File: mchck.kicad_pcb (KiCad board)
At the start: 2 copper layers, 36.6 x 18.8 mm, 41 parts, among them J3 MICRO_USB, P1 RIGHT_PINS, P10 GND, P11 D-, P12 D+, P2 DEBUG, P3 UPPER_PINS, P4 LOWER_PINS, P5 CHG, P7 LIPO, P9 5V, U1 MK20LF, U2 MCP73831-SOT, U3 SPI_FLASH-X25XXSMD, U4 MULTIREG, Y1 CRYSTAL32-SMD

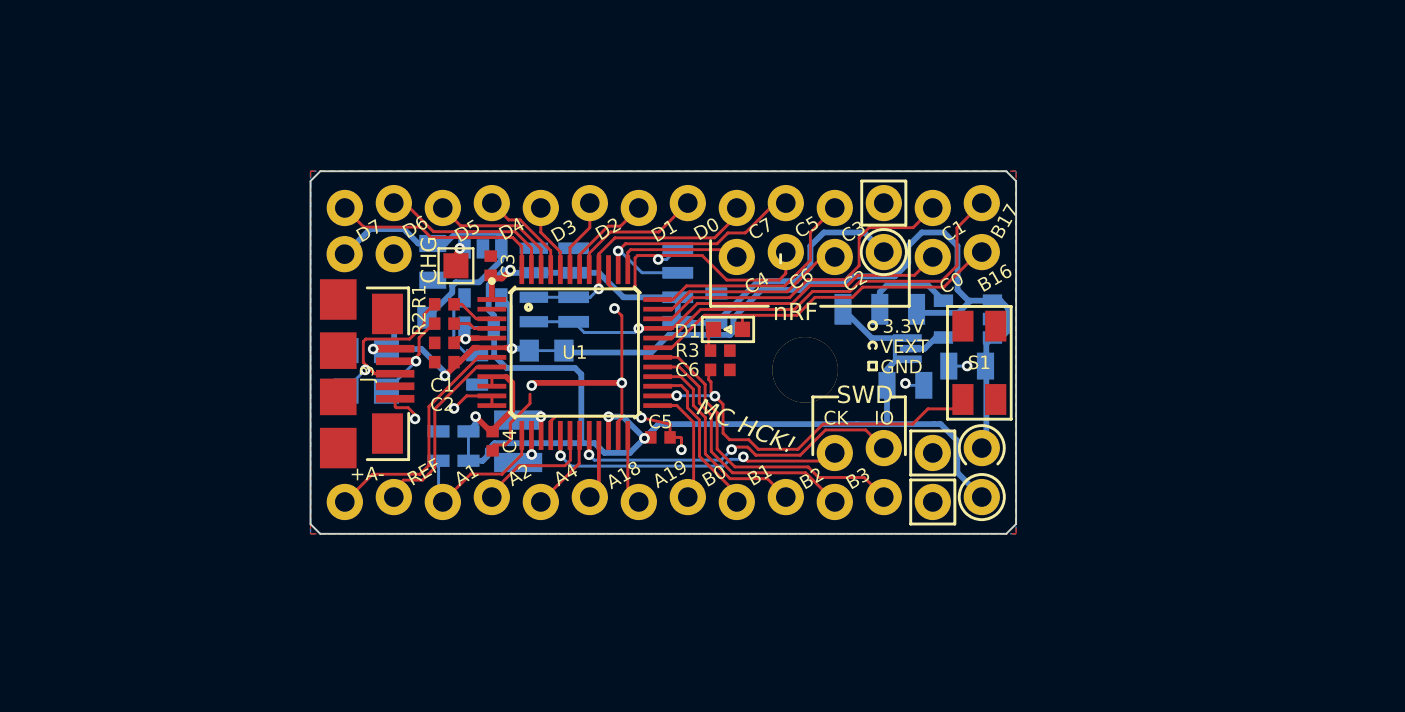
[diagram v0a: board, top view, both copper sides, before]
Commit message: Mash up of MCHCK with TinyK20-like pinout
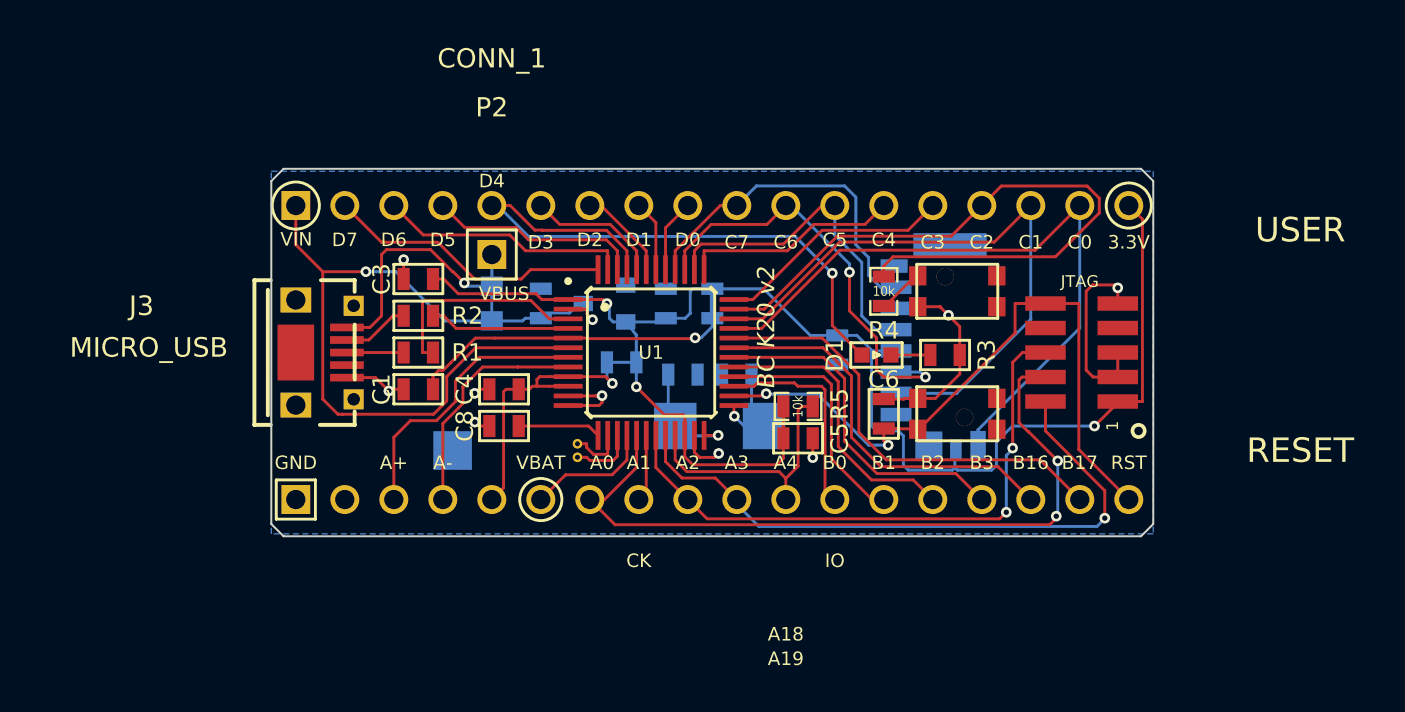
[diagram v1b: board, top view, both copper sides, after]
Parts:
- removed C10: 100n, SM0603_Capa
- removed C7: 4.7u, SM0805
- removed D2: CDBU0530, SOD-523F
- removed H1: MOUNTHOLE, mounthole_3mm
- removed L1: INDUCTOR_SELECT, SM0805-3WAY
- removed P1: RIGHT_PINS, SparkFun-1X06_LOCK
- removed P10: GND, solderpad
- removed P11: D-, solderpad
- removed P12: D+, solderpad
- removed P5: CHG, solderpad
- removed P7: LIPO, SIL100-2
- removed P9: 5V, solderpad
- removed SJ5: SOLDERJUMPERNO, solder-jumper
- removed U3: SPI_FLASH-X25XXSMD, SparkFun-SO08
- removed U4: MULTIREG, SOT23-5
- added C13: 18pF, SM0603_Capa, B.Cu at (61.0, 51.9)
- added C9: 18pF, SM0603_Capa, B.Cu at (58.2, 51.9)
- added K1: CONN_MICROSD, SD_MOLEX_47579-0001-2, B.Cu at (69.2, 50.2)
- added M1: PCB_GREEN_RMC, PCB_GREEN, F.Cu at (59.7, 50.8)
- added P6: JTAG, Pin_Array_5x2_SMT_1.27mm_RMC, F.Cu at (78.7, 50.8)
- added R5: 10k, SM0603_Resistor, F.Cu at (64.1, 53.6)
- added S2: USER, SW_C&K_KMR4_ALT, F.Cu at (72.4, 47.6)
- added X1: 8MHz, XTAL-SM-TXC-7A, B.Cu at (60.1, 54.6)
- C1, C3, C4, C5, C6: footprint SMD-1005 -> SM0603_Capa
- C11, C12: footprint SM0805 -> SM0603_Capa
- C2: value 2.2u -> 100n; footprint SMD-1005 -> SM0603_Capa; moved to B.Cu
- C8: moved to F.Cu
- D3: value CDBU0530 -> DIODE-SCHOTTKY_
- J3: footprint SparkFun-USB-MICROB -> USB_MICRO_RMC_FCI
- P2: value DEBUG -> CONN_1; footprint SparkFun-1X04_LOCK -> pin_header_2.54mm_1x1; moved to F.Cu
- P3, P4: footprint SparkFun-1X14_LOCK -> pin_header_2.54mm_1x18
- R1, R2, R3: footprint SMD-1005 -> SM0603
- R4: value 20k -> 10k; footprint SM0603 -> SM0603_Resistor; moved to F.Cu
- S1: value TAC_SWITCHSMD_EVQP2 -> RESET; footprint TACT_4x3 -> SW_C&K_KMR4_ALT
- SJ6: footprint SM0603_NC -> SM0603_Bridged
- U2: value MCP73831-SOT -> MCP1703_SOT23; footprint SOT23-5 -> SOT23
- Y1: value CRYSTAL32-SMD -> 32.768kHz; footprint SparkFun-CRYSTAL-32KHZ-SMD -> crystal_tc-26_horiz
- moved C12 22.3 mm to (50.8, 48.3), turned to 90 degrees
- moved R4 21.5 mm to (68.6, 47.6)
- moved P2 20.5 mm to (48.3, 45.7)
- moved C2 20.4 mm to (66.2, 50.7)
- moved G1 19.8 mm to (77.5, 50.2)
- moved P3 19.0 mm to (59.7, 43.2)
- moved P4 19.0 mm to (59.7, 58.4)
- moved C11 13.1 mm to (57.3, 48.3), turned to 90 degrees
- moved SJ6 12.2 mm to (59.7, 48.3), turned to 90 degrees
- moved R3 11.7 mm to (71.8, 50.9), turned to 0 degrees
- moved FB1 9.05 mm to (55.0, 51.3), turned to 180 degrees
- moved C6 8.78 mm to (68.6, 54.0)
- moved D1 7.81 mm to (68.2, 50.9), turned to 0 degrees
- moved C5 7.14 mm to (64.1, 55.2), turned to 0 degrees
- moved U2 6.49 mm to (54.1, 48.3), turned to 270 degrees
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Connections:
- net /MCU/USB_DM renamed USB_DM
- net /MCU/USB_DP renamed USB_DP
- net /MCU/VREGUSB renamed VREG_K20
- C12 pad 1: /power/VRAW -> VRAW
- C2 pad 1: /MCU/+5V -> VDD
- C4 pad 1: VDDA -> VREFH
- C6 pad 1: N-0000047 -> RST
- C8 pad 1: /MCU/PL3 -> N-0000053
- D1 pad 1: /MCU/PR6 -> D4
- D3 pad A: /MCU/+5V -> VBUS
- D3 pad C: /power/VRAW -> VRAW
- FB1 pad 2: VDDA -> VREFH
- J3 pad 1: /MCU/+5V -> VBUS
- J3 pad 4: (no net) -> VSS
- J3 pad 5: VSS -> (no net)
- P2 pad 1: /MCU/SWD_CLK -> VBUS
- P3 pad 1: /MCU/PU1 -> VRAW
- P3 pad 10: /MCU/PU10 -> C7
- P3 pad 11: /MCU/PU11 -> C6
- P3 pad 12: VSS -> C5
- P3 pad 13: /MCU/PU13 -> C4
- P3 pad 14: /MCU/PU14 -> C3
- P3 pad 2: /MCU/PU2 -> D7
- P3 pad 3: /MCU/PU3 -> D6
- P3 pad 4: /MCU/PU4 -> D5
- P3 pad 5: /MCU/PU5 -> D4
- P3 pad 6: /MCU/PU6 -> D3
- P3 pad 7: /MCU/PU7 -> D2
- P3 pad 8: /MCU/PU8 -> D1
- P3 pad 9: /MCU/PU9 -> D0
- P4 pad 1: /MCU/PL1 -> VSS
- P4 pad 10: /MCU/PL10 -> A3
- P4 pad 11: /MCU/PL11 -> A4
- P4 pad 12: /MCU/PL12 -> B0
- P4 pad 13: VSS -> B1
- P4 pad 14: VDD -> B2
- P4 pad 2: /MCU/PL2 -> (no net)
- P4 pad 3: /MCU/PL3 -> ADC0+
- P4 pad 4: /MCU/PL4 -> ADC0-
- P4 pad 5: /MCU/PL5 -> VREFH
- P4 pad 6: /MCU/PL6 -> VBAT
- P4 pad 7: /MCU/PL7 -> A0
- P4 pad 8: /MCU/PL8 -> A1
- P4 pad 9: /MCU/PL9 -> A2
- R4 pad 1: N-0000041 -> C2
- R4 pad 2: VSS -> N-0000054
- S1 pad 1: N-0000047 -> (no net)
- S1 pad 2: VSS -> (no net)
- S1 pad 3: (no net) -> RST
- U1 pad 10: VDDA -> VREFH
- U1 pad 13: /MCU/PL3 -> N-0000053
- U1 pad 14: N-0000046 -> N-0000047
- U1 pad 15: N-0000050 -> N-0000046
- U1 pad 16: VDD -> VBAT
- U1 pad 17: /MCU/SWD_CLK -> A0
- U1 pad 18: /MCU/PL4 -> A1
- U1 pad 19: /MCU/PL5 -> A2
- U1 pad 20: /MCU/SWD_DIO -> A3
- U1 pad 21: /MCU/PL6 -> A4
- U1 pad 24: /MCU/PL7 -> A18
- U1 pad 25: /MCU/PL8 -> A19
- U1 pad 26: N-0000047 -> RST
- U1 pad 27: /MCU/PL9 -> B0
- U1 pad 28: /MCU/PL10 -> B1
- U1 pad 29: /MCU/PL11 -> B2
- U1 pad 30: /MCU/PL12 -> B3
- U1 pad 31: /MCU/PR6 -> B16
- U1 pad 32: /MCU/PU14 -> B17
- U1 pad 33: /MCU/PR5 -> C0
- U1 pad 34: /MCU/PU13 -> C1
- U1 pad 35: /MCU/PR3 -> C2
- U1 pad 36: /MCU/PU11 -> C3
- U1 pad 37: /MCU/PR1 -> C4
- U1 pad 38: /MCU/PU10 -> C5
- U1 pad 39: /MCU/PR2 -> C6
- U1 pad 40: /MCU/PU9 -> C7
- U1 pad 41: /MCU/PU8 -> D0
- U1 pad 42: /MCU/PU7 -> D1
- U1 pad 43: /MCU/PU6 -> D2
- U1 pad 44: /MCU/PU5 -> D3
- U1 pad 45: /MCU/PU4 -> D4
- U1 pad 46: /MCU/PU3 -> D5
- U1 pad 47: /MCU/PU2 -> D6
- U1 pad 48: /MCU/PU1 -> D7
- U1 pad 6: /MCU/+5V -> VRAW
- U1 pad 7: /MCU/PL1 -> ADC0+
- U1 pad 8: /MCU/PL2 -> ADC0-
- U1 pad 9: VDDA -> VREFH
- U2 pad 1: N-0000040 -> VSS
- U2 pad 2: VSS -> VDD
- U2 pad 3: /power/VLIPO -> VRAW
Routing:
- net VRAW: track 0.00 -> 40.9 mm, vias 0 -> 1
- net /power/VRAW: track 40.8 -> 0.00 mm
- net A0: track 0.00 -> 39.1 mm, vias 0 -> 2
- net C2: track 0.00 -> 35.5 mm
- net C0: track 0.00 -> 35.2 mm
- net RST: track 0.00 -> 35.1 mm, vias 0 -> 2
- net A3: track 0.00 -> 33.2 mm, vias 0 -> 1
- net D4: track 0.00 -> 33.0 mm, vias 0 -> 1
- net C1: track 0.00 -> 32.3 mm
- net A2: track 0.00 -> 30.9 mm, vias 0 -> 2
- net B17: track 0.00 -> 23.1 mm
- net /MCU/PR5: track 22.5 -> 0.00 mm, vias 1 -> 0
- net C6: track 0.00 -> 22.1 mm, vias 0 -> 2
- net /MCU/PU14: track 20.8 -> 0.00 mm
- net B16: track 0.00 -> 20.5 mm
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- removed copper zone on F.Cu, net VSS
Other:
- board size 36.6 x 18.8 mm -> 45.7 x 19.1 mm
- net class Power: clearance 0.14986 -> 0.1524; trace_width 0.29972 -> 0.1524
- rule trace_min: 0.0002 -> 0.1524
- rule via_min_size: 0.0008 -> 0.5334
- board text added: "A+"
- board text added: "A-"
- board text added: "A0"
- board text added: "A3"
- board text added: "BC K20 v2"
- board text added: "RST"
- board text added: "VBAT"
- board text added: "VBUS"
- board text added: "VIN"
- board text added: "open hardware"
- board text removed: "+A-"
- board text removed: "MC HCK!"
- board text removed: "R5 rc3"
- board text removed: "REF"
- board text removed: "SWD"
- board text removed: "VEXT"
- board text removed: "mchck.org"
- board text removed: "nRF"

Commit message: Fix up libs and footprints for Kicad v4; remove several unused libs
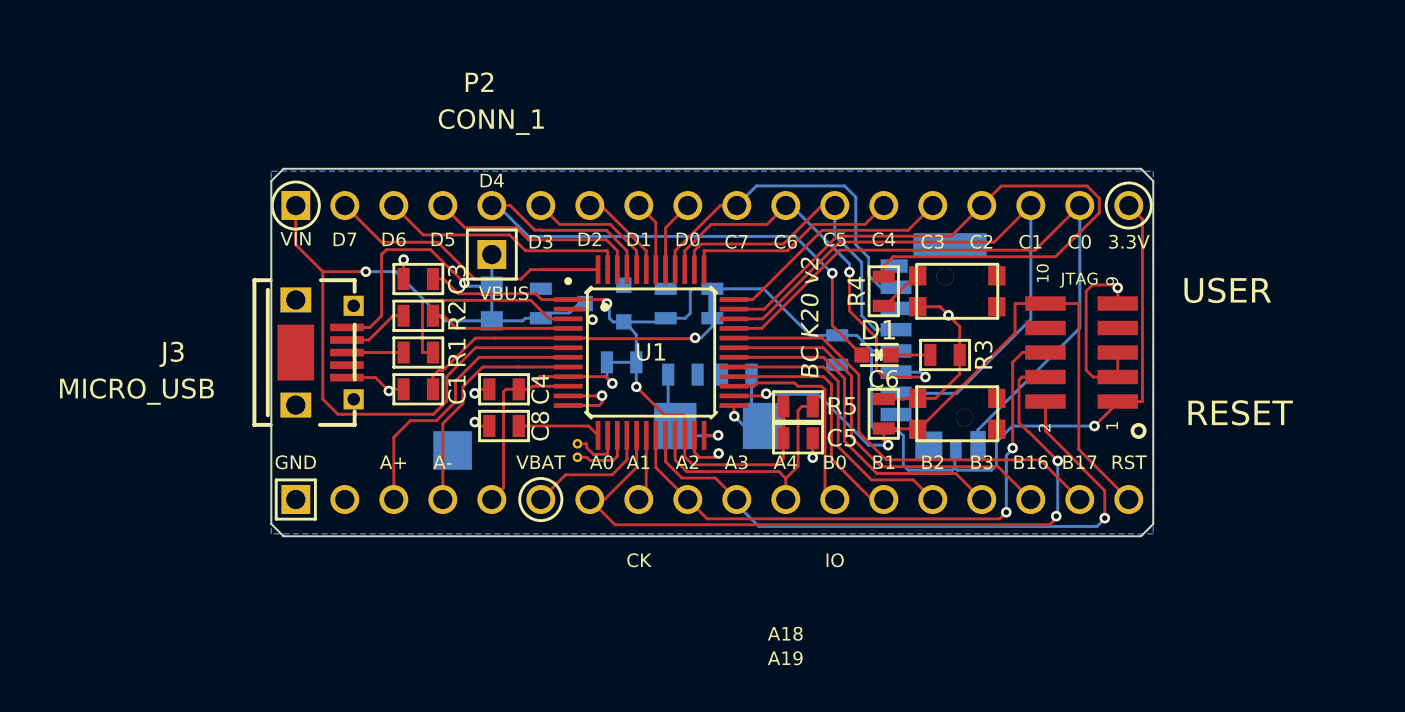
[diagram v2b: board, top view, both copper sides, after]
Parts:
- removed M1: PCB_GREEN_RMC, PCB_GREEN
- C1, C11, C12, C13, C2, C3, C4, C5, C6, C8, C9: footprint SM0603_Capa -> mchck:SM0603_Capa
- D1: footprint LED-0603 -> LEDs:LED-0603
- D3: footprint SOD-523F-NC -> mchck:SOD-523F-NC
- FB1: footprint SM0603_NC -> mchck:SM0603_NC
- G1: footprint OHW-LOGO-6mm -> mchck:OHW-LOGO-6mm
- J3: footprint USB_MICRO_RMC_FCI -> RMC:USB_MICRO_RMC_FCI
- K1: footprint SD_MOLEX_47579-0001-2 -> RMC:SD_MOLEX_47579-0001-2
- P2: footprint pin_header_2.54mm_1x1 -> RMC_pcb_header:pin_header_2.54mm_1x1
- P3, P4: footprint pin_header_2.54mm_1x18 -> RMC_pcb_header:pin_header_2.54mm_1x18
- P6: footprint Pin_Array_5x2_SMT_1.27mm_RMC -> RMC:Pin_Array_5x2_SMT_1.27mm_RMC
- R1, R2, R3: footprint SM0603 -> mchck:SM0603
- R4, R5: footprint SM0603_Resistor -> mchck:SM0603
- S1, S2: footprint SW_C&K_KMR4_ALT -> RMC:SW_C&K_KMR4_ALT
- SJ6: footprint SM0603_Bridged -> RMC:SM0603_Bridged
- U1: footprint LQFP48 -> mchck:LQFP48
- U2: footprint SOT23 -> TO_SOT_Packages_SMD:SOT-23
- X1: footprint XTAL-SM-TXC-7A -> RMC:XTAL-SM-TXC-7A
- Y1: footprint crystal_tc-26_horiz -> w_crystal:crystal_tc-26_horiz
- turned D1 to 180 degrees
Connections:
- net VSS renamed GND
- D1 pad 1: D4 -> Net-(D1-Pad1)
- D1 pad 2: N-0000045 -> D4
- J3 pad 5: (no net) -> Net-(J3-Pad5)
- J3 pad 6: (no net) -> Net-(J3-Pad6)
- K1 pad 1: (no net) -> Net-(K1-Pad1)
- K1 pad 8: (no net) -> Net-(K1-Pad8)
- P4 pad 2: (no net) -> Net-(P4-Pad2)
- P6 pad 7: (no net) -> Net-(P6-Pad7)
- P6 pad 8: (no net) -> Net-(P6-Pad8)
- R3 pad 1: N-0000045 -> Net-(D1-Pad1)
- S1 pad 1: (no net) -> Net-(S1-Pad1)
- S1 pad 2: (no net) -> Net-(S1-Pad2)
- S2 pad 3: (no net) -> Net-(S2-Pad3)
- S2 pad 4: (no net) -> Net-(S2-Pad4)
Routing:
- net Net-(D1-Pad1): track 0.00 -> 2.04 mm
- net N-0000045: track 2.04 -> 0.00 mm

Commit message: Tidy up some texts; add doc files
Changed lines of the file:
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@@
     (links 113)
     (no_connects 4)
-    (area 15.669442 24.431499 94.582591 67.23993)
+    (area 36.779199 41.224199 82.600801 60.375801)
     (thickness 1.6002)
     (drawings 65)
     (tracks 495)
     (zones 0)
-    (modules 34)
+    (modules 33)
     (nets 60)
   )
@@
     (aux_axis_origin 36.83 60.325)
     (grid_origin 36.83 60.325)
-    (visible_elements 7FFCD61F)
+    (visible_elements 7FFFD67F)
     (pcbplotparams
       (layerselection 0x010f0_80000001)
@@
       (net 43 GND))
     (model Capacitors_SMD.3dshapes/C_0603.wrl
-      (at (xyz 0 0 0.0))
-      (scale (xyz 1.0 1.0 1.0))
+      (at (xyz 0 0 0))
+      (scale (xyz 1 1 1))
       (rotate (xyz 0 0 0))
     )
@@
       (net 43 GND))
     (model Capacitors_SMD.3dshapes/C_0603.wrl
-      (at (xyz 0 0 0.0))
-      (scale (xyz 1.0 1.0 1.0))
+      (at (xyz 0 0 0))
+      (scale (xyz 1 1 1))
       (rotate (xyz 0 0 0))
     )
@@
       (net 43 GND))
     (model Capacitors_SMD.3dshapes/C_0603.wrl
-      (at (xyz 0 0 0.0))
-      (scale (xyz 1.0 1.0 1.0))
+      (at (xyz 0 0 0))
+      (scale (xyz 1 1 1))
       (rotate (xyz 0 0 0))
     )
@@
       (net 43 GND))
     (model Capacitors_SMD.3dshapes/C_0603.wrl
-      (at (xyz 0 0 0.0))
-      (scale (xyz 1.0 1.0 1.0))
+      (at (xyz 0 0 0))
+      (scale (xyz 1 1 1))
       (rotate (xyz 0 0 0))
     )
@@
       (net 43 GND))
     (model Capacitors_SMD.3dshapes/C_0603.wrl
-      (at (xyz 0 0 0.0))
-      (scale (xyz 1.0 1.0 1.0))
+      (at (xyz 0 0 0))
+      (scale (xyz 1 1 1))
       (rotate (xyz 0 0 0))
     )
@@
       (net 43 GND))
     (model Capacitors_SMD.3dshapes/C_0603.wrl
-      (at (xyz 0 0 0.0))
-      (scale (xyz 1.0 1.0 1.0))
+      (at (xyz 0 0 0))
+      (scale (xyz 1 1 1))
       (rotate (xyz 0 0 0))
     )
@@
       (net 43 GND))
     (model Capacitors_SMD.3dshapes/C_0603.wrl
-      (at (xyz 0 0 0.0))
-      (scale (xyz 1.0 1.0 1.0))
+      (at (xyz 0 0 0))
+      (scale (xyz 1 1 1))
       (rotate (xyz 0 0 0))
     )
@@
       (net 43 GND))
     (model Capacitors_SMD.3dshapes/C_0603.wrl
-      (at (xyz 0 0 0.0))
-      (scale (xyz 1.0 1.0 1.0))
+      (at (xyz 0 0 0))
+      (scale (xyz 1 1 1))
       (rotate (xyz 0 0 0))
     )
@@
       (net 43 GND))
     (model Capacitors_SMD.3dshapes/C_0603.wrl
-      (at (xyz 0 0 0.0))
-      (scale (xyz 1.0 1.0 1.0))
+      (at (xyz 0 0 0))
+      (scale (xyz 1 1 1))
       (rotate (xyz 0 0 0))
     )
@@
       (net 43 GND))
     (model Capacitors_SMD.3dshapes/C_0603.wrl
-      (at (xyz 0 0 0.0))
-      (scale (xyz 1.0 1.0 1.0))
+      (at (xyz 0 0 0))
+      (scale (xyz 1 1 1))
       (rotate (xyz 0 0 0))
     )
@@
       (net 43 GND))
     (model Capacitors_SMD.3dshapes/C_0603.wrl
-      (at (xyz 0 0 0.0))
-      (scale (xyz 1.0 1.0 1.0))
+      (at (xyz 0 0 0))
+      (scale (xyz 1 1 1))
       (rotate (xyz 0 0 0))
     )
@@
   (module RMC:USB_MICRO_RMC_FCI (layer F.Cu)
     (at 38.1 50.8)
-    (fp_text reference J3 (at -6.35 0) (layer F.SilkS)
+    (fp_text reference J3 (at -8.89 0) (layer F.SilkS) hide
       (effects (font (size 1.016 1.016) (thickness 0.127)))
     )
-    (fp_text value MICRO_USB (at -8.255 1.905) (layer F.SilkS)
+    (fp_text value MICRO_USB (at -5.461 0.127 90) (layer F.SilkS)
       (effects (font (size 1.016 1.016) (thickness 0.127)))
     )
@@
   (module RMC:SD_MOLEX_47579-0001-2 (layer B.Cu)
     (at 69.215 50.165 270)
-    (fp_text reference K1 (at -11.43 0 270) (layer B.SilkS)
+    (fp_text reference K1 (at -11.43 0 270) (layer B.SilkS) hide
       (effects (font (size 1 1) (thickness 0.15)) (justify mirror))
     )
-    (fp_text value CONN_MICROSD (at 0 -16.51 270) (layer B.SilkS)
+    (fp_text value CONN_MICROSD (at 0.635 -22.86 270) (layer B.SilkS) hide
       (effects (font (size 1 1) (thickness 0.15)) (justify mirror))
     )
@@
   (module RMC_pcb_header:pin_header_2.54mm_1x1 (layer F.Cu)
     (at 48.26 45.72)
-    (fp_text reference P2 (at -0.635 -8.89) (layer F.SilkS)
+    (fp_text reference P2 (at -0.635 -8.89) (layer F.SilkS) hide
       (effects (font (size 1 1) (thickness 0.15)))
     )
-    (fp_text value CONN_1 (at 0 -6.985) (layer F.SilkS)
+    (fp_text value CONN_1 (at 0 -6.985) (layer F.SilkS) hide
       (effects (font (size 1 1) (thickness 0.15)))
     )
@@
   (module RMC_pcb_header:pin_header_2.54mm_1x18 (layer B.Cu)
     (at 59.69 43.18)
-    (fp_text reference P3 (at 0 -6.35) (layer B.SilkS)
+    (fp_text reference P3 (at 0 -6.35) (layer B.SilkS) hide
       (effects (font (size 1 1) (thickness 0.15)) (justify mirror))
     )
-    (fp_text value UPPER_PINS (at -6.35 -6.35) (layer B.SilkS)
+    (fp_text value UPPER_PINS (at -6.35 -6.35) (layer B.SilkS) hide
       (effects (font (size 1 1) (thickness 0.15)) (justify mirror))
     )
@@
   (module RMC_pcb_header:pin_header_2.54mm_1x18 (layer B.Cu)
     (at 59.69 58.42)
-    (fp_text reference P4 (at -0.635 5.715) (layer B.SilkS)
+    (fp_text reference P4 (at -0.635 5.715) (layer B.SilkS) hide
       (effects (font (size 1 1) (thickness 0.15)) (justify mirror))
     )
-    (fp_text value LOWER_PINS (at -6.985 5.715) (layer B.SilkS)
+    (fp_text value LOWER_PINS (at -6.985 5.715) (layer B.SilkS) hide
       (effects (font (size 1 1) (thickness 0.15)) (justify mirror))
     )
@@
       (net 36 USB_DP))
     (model Resistors_SMD.3dshapes/R_0603.wrl
-      (at (xyz 0 0 0.0))
-      (scale (xyz 1.0 1.0 1.0))
+      (at (xyz 0 0 0))
+      (scale (xyz 1 1 1))
       (rotate (xyz 0 0 0))
     )
@@
       (net 35 USB_DM))
     (model Resistors_SMD.3dshapes/R_0603.wrl
-      (at (xyz 0 0 0.0))
-      (scale (xyz 1.0 1.0 1.0))
+      (at (xyz 0 0 0))
+      (scale (xyz 1 1 1))
       (rotate (xyz 0 0 0))
     )
@@
       (net 43 GND))
     (model Resistors_SMD.3dshapes/R_0603.wrl
-      (at (xyz 0 0 0.0))
-      (scale (xyz 1.0 1.0 1.0))
+      (at (xyz 0 0 0))
+      (scale (xyz 1 1 1))
       (rotate (xyz 0 0 0))
     )
@@
       (net 52 "Net-(R4-Pad2)"))
     (model Resistors_SMD.3dshapes/R_0603.wrl
-      (at (xyz 0 0 0.0))
-      (scale (xyz 1.0 1.0 1.0))
+      (at (xyz 0 0 0))
+      (scale (xyz 1 1 1))
       (rotate (xyz 0 0 0))
     )
@@
       (net 9 A4))
     (model Resistors_SMD.3dshapes/R_0603.wrl
-      (at (xyz 0 0 0.0))
-      (scale (xyz 1.0 1.0 1.0))
+      (at (xyz 0 0 0))
+      (scale (xyz 1 1 1))
       (rotate (xyz 0 0 0))
     )
@@
       (effects (font (size 0.50038 0.4572) (thickness 0.1143)) (justify mirror))
     )
-    (fp_text value SOLDERJUMPERNC (at 8.89 3.175 360) (layer B.SilkS)
+    (fp_text value SOLDERJUMPERNC (at 8.89 3.175 180) (layer B.SilkS) hide
       (effects (font (size 0.508 0.4572) (thickness 0.1143)) (justify mirror))
     )
@@
       (effects (font (thickness 0.2032)) (justify mirror))
     )
-    (fp_text value 8MHz (at 16.129 8.89) (layer B.SilkS)
+    (fp_text value 8MHz (at 16.129 8.89) (layer B.SilkS) hide
       (effects (font (thickness 0.2032)) (justify mirror))
     )
